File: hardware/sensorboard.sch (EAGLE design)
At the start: 37 parts, among them U1 LM1117MP-3.3, U2 LM324D

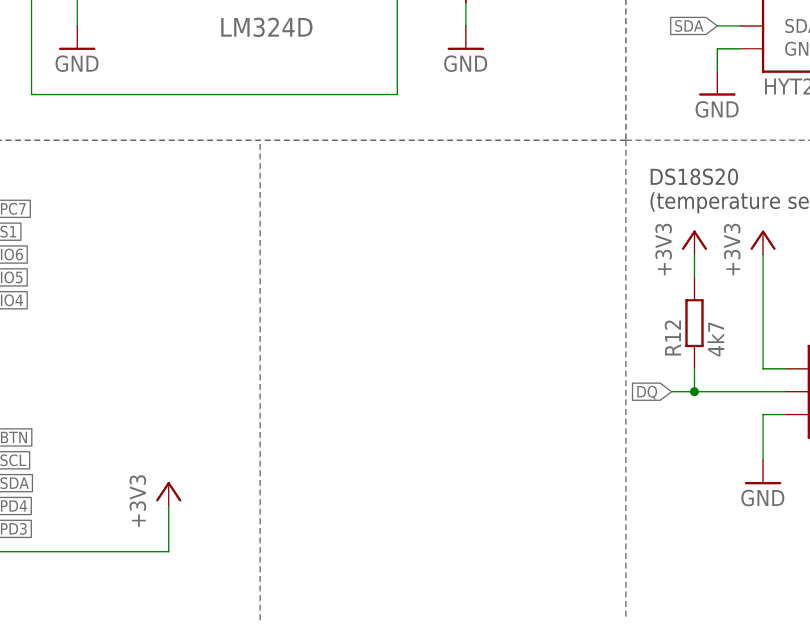
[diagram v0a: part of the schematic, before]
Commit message: added I2C pull up resistors
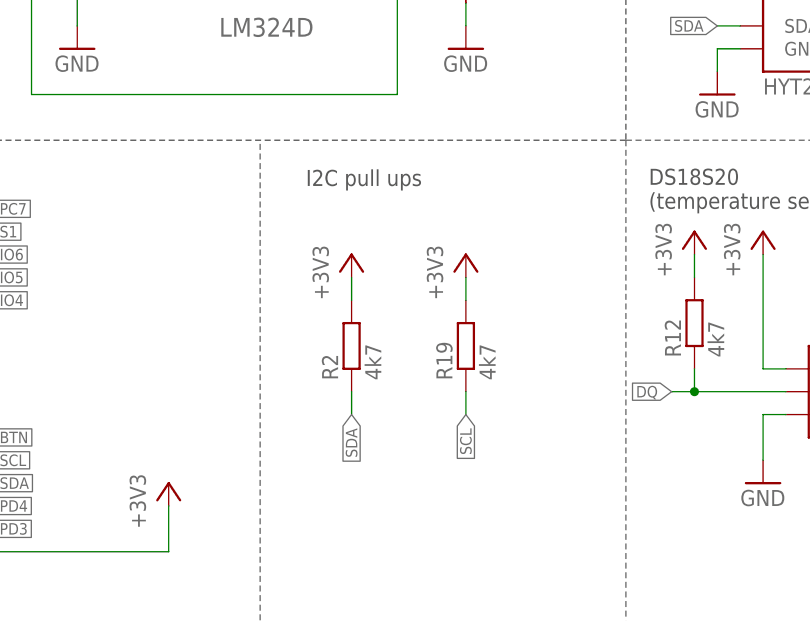
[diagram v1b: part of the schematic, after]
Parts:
- added R19, R2: 4k7, rcl:R-EU_R0805
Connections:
- net +3V3: now also R19.2, R2.2
- net SCL: now also R19.1
- net SDA: now also R2.1
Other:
- note added: "I2C pull ups"
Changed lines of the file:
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@@
 <part name="U$5" library="dallas" deviceset="DS18S20" device=""/>
 <part name="U$3" library="humidity" deviceset="BMP085" device=""/>
+<part name="+3V12" library="supply1" deviceset="+3V3" device=""/>
+<part name="+3V13" library="supply1" deviceset="+3V3" device=""/>
+<part name="R2" library="rcl" deviceset="R-EU_" device="R0805" value="4k7"/>
+<part name="R19" library="rcl" deviceset="R-EU_" device="R0805" value="4k7"/>
 </parts>
 <sheets>
@@
 <wire x1="220.98" y1="78.74" x2="162.56" y2="78.74" width="0.1524" layer="97" style="longdash"/>
 <text x="167.64" y="76.2" size="1.27" layer="97">connectors#</text>
+<text x="93.98" y="53.34" size="1.778" layer="97">I2C pull ups</text>
 </plain>
 <instances>
@@
 <instance part="U$5" gate="G$1" x="154.94" y="30.48"/>
 <instance part="U$3" gate="G$1" x="154.94" y="116.84"/>
+<instance part="+3V12" gate="G$1" x="99.06" y="45.72"/>
+<instance part="+3V13" gate="G$1" x="111.76" y="45.72"/>
+<instance part="R2" gate="G$1" x="99.06" y="35.56" rot="R90"/>
+<instance part="R19" gate="G$1" x="111.76" y="35.56" rot="R90"/>
 </instances>
 <busses>
@@
 <wire x1="134.62" y1="121.92" x2="134.62" y2="124.46" width="0.1524" layer="91"/>
 </segment>
+<segment>
+<pinref part="+3V12" gate="G$1" pin="+3V3"/>
+<pinref part="R2" gate="G$1" pin="2"/>
+<wire x1="99.06" y1="43.18" x2="99.06" y2="40.64" width="0.1524" layer="91"/>
+</segment>
+<segment>
+<pinref part="+3V13" gate="G$1" pin="+3V3"/>
+<pinref part="R19" gate="G$1" pin="2"/>
+<wire x1="111.76" y1="43.18" x2="111.76" y2="40.64" width="0.1524" layer="91"/>
+</segment>
 </net>
 <net name="+5V" class="0">
@@
 <label x="144.78" y="111.76" size="1.27" layer="95" rot="R180" xref="yes"/>
 </segment>
+<segment>
+<pinref part="R2" gate="G$1" pin="1"/>
+<wire x1="99.06" y1="30.48" x2="99.06" y2="27.94" width="0.1524" layer="91"/>
+<label x="99.06" y="27.94" size="1.27" layer="95" rot="R270" xref="yes"/>
+</segment>
 </net>
 <net name="SCL" class="0">
@@
 <label x="144.78" y="114.3" size="1.27" layer="95" rot="R180" xref="yes"/>
 </segment>
-</net>
+<segment>
+<pinref part="R19" gate="G$1" pin="1"/>
+<wire x1="111.76" y1="30.48" x2="111.76" y2="27.94" width="0.1524" layer="91"/>
+<label x="111.76" y="27.94" size="1.27" layer="95" rot="R270" xref="yes"/>
+</segment>
+</net>

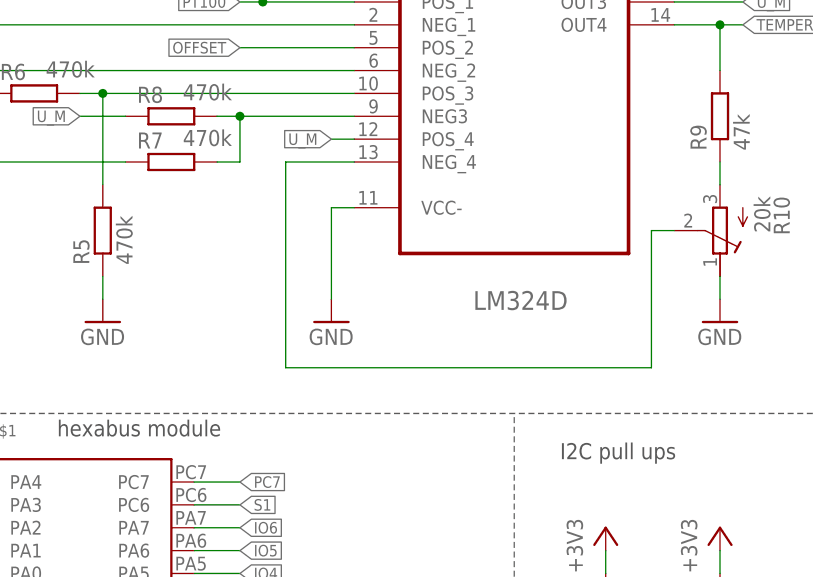
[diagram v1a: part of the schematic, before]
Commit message: added a pinheader for calibrating the measure amplifier. fixes #2
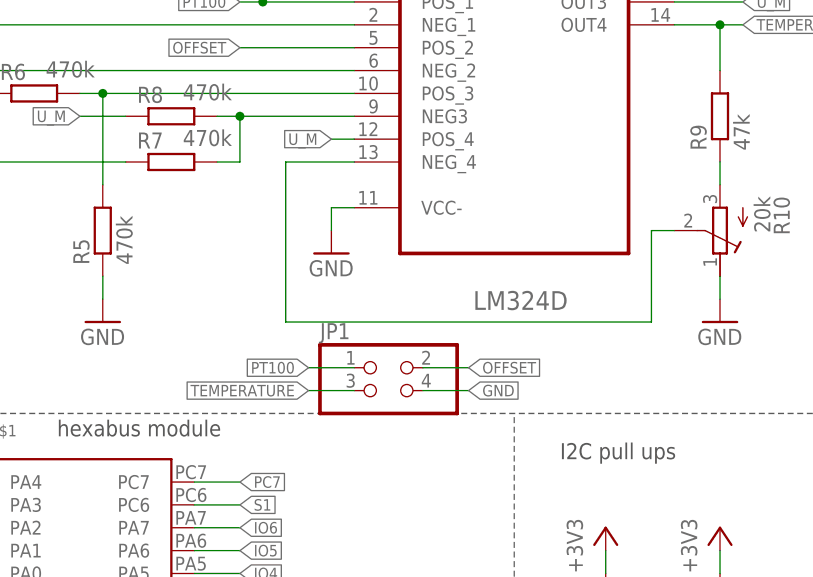
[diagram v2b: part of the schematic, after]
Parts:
- added JP1: (no value), pinhead:PINHD-2X2
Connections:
- net GND: now also JP1.4
- net OFFSET: now also JP1.2
- net PT100: now also JP1.1
- net TEMPERATURE: now also JP1.3
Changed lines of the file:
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@@
 <part name="R2" library="rcl" deviceset="R-EU_" device="R0805" value="4k7"/>
 <part name="R19" library="rcl" deviceset="R-EU_" device="R0805" value="4k7"/>
+<part name="JP1" library="pinhead" deviceset="PINHD-2X2" device=""/>
 </parts>
 <sheets>
@@
 <instance part="U2" gate="A" x="88.9" y="99.06"/>
 <instance part="+3V4" gate="G$1" x="68.58" y="121.92"/>
-<instance part="GND5" gate="1" x="68.58" y="68.58"/>
+<instance part="GND5" gate="1" x="68.58" y="76.2"/>
 <instance part="+3V5" gate="G$1" x="60.96" y="121.92"/>
 <instance part="GND6" gate="1" x="43.18" y="68.58"/>
@@
 <instance part="R2" gate="G$1" x="99.06" y="35.56" rot="R90"/>
 <instance part="R19" gate="G$1" x="111.76" y="35.56" rot="R90"/>
+<instance part="JP1" gate="A" x="76.2" y="60.96"/>
 </instances>
 <busses>
@@
 <pinref part="GND5" gate="1" pin="GND"/>
 <wire x1="71.12" y1="81.28" x2="68.58" y2="81.28" width="0.1524" layer="91"/>
-<wire x1="68.58" y1="81.28" x2="68.58" y2="71.12" width="0.1524" layer="91"/>
+<wire x1="68.58" y1="81.28" x2="68.58" y2="78.74" width="0.1524" layer="91"/>
 </segment>
 <segment>
@@
 <wire x1="139.7" y1="109.22" x2="139.7" y2="104.14" width="0.1524" layer="91"/>
 </segment>
+<segment>
+<pinref part="JP1" gate="A" pin="4"/>
+<wire x1="78.74" y1="60.96" x2="83.82" y2="60.96" width="0.1524" layer="91"/>
+<label x="83.82" y="60.96" size="1.27" layer="95" xref="yes"/>
+</segment>
 </net>
 <net name="+3V3" class="0">
@@
 <label x="182.88" y="55.88" size="1.27" layer="95" rot="R180" xref="yes"/>
 </segment>
+<segment>
+<pinref part="JP1" gate="A" pin="1"/>
+<wire x1="71.12" y1="63.5" x2="66.04" y2="63.5" width="0.1524" layer="91"/>
+<label x="66.04" y="63.5" size="1.27" layer="95" rot="R180" xref="yes"/>
+</segment>
 </net>
 <net name="OFFSET" class="0">
@@
 <wire x1="10.16" y1="101.6" x2="7.62" y2="101.6" width="0.1524" layer="91"/>
 <label x="7.62" y="101.6" size="1.27" layer="95" rot="R90" xref="yes"/>
+</segment>
+<segment>
+<pinref part="JP1" gate="A" pin="2"/>
+<wire x1="78.74" y1="63.5" x2="83.82" y2="63.5" width="0.1524" layer="91"/>
+<label x="83.82" y="63.5" size="1.27" layer="95" xref="yes"/>
 </segment>
 </net>
@@
 <label x="22.86" y="50.8" size="1.27" layer="95" rot="R180" xref="yes"/>
 </segment>
+<segment>
+<pinref part="JP1" gate="A" pin="3"/>
+<wire x1="71.12" y1="60.96" x2="66.04" y2="60.96" width="0.1524" layer="91"/>
+<label x="66.04" y="60.96" size="1.27" layer="95" rot="R180" xref="yes"/>
+</segment>
 </net>
 <net name="N$6" class="0">
@@
 <pinref part="R10" gate="G$1" pin="S"/>
 <wire x1="106.68" y1="78.74" x2="104.14" y2="78.74" width="0.1524" layer="91"/>
-<wire x1="104.14" y1="78.74" x2="104.14" y2="63.5" width="0.1524" layer="91"/>
-<wire x1="104.14" y1="63.5" x2="63.5" y2="63.5" width="0.1524" layer="91"/>
+<wire x1="104.14" y1="78.74" x2="104.14" y2="68.58" width="0.1524" layer="91"/>
+<wire x1="104.14" y1="68.58" x2="63.5" y2="68.58" width="0.1524" layer="91"/>
 <pinref part="U2" gate="A" pin="NEG_4"/>
-<wire x1="63.5" y1="63.5" x2="63.5" y2="86.36" width="0.1524" layer="91"/>
+<wire x1="63.5" y1="68.58" x2="63.5" y2="86.36" width="0.1524" layer="91"/>
 <wire x1="63.5" y1="86.36" x2="71.12" y2="86.36" width="0.1524" layer="91"/>
 </segment>

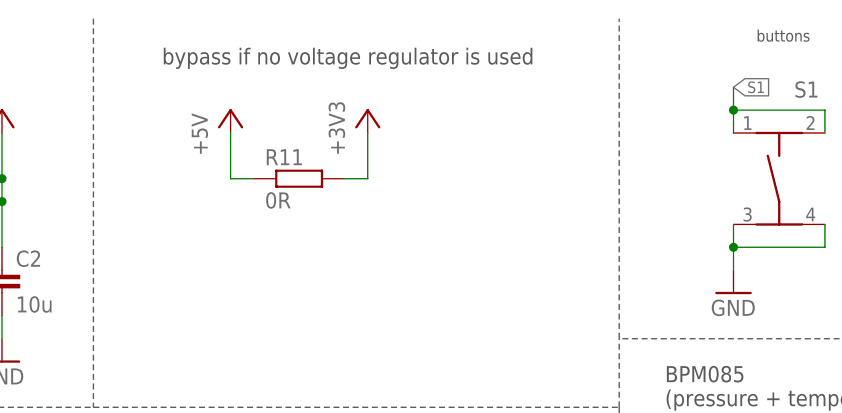
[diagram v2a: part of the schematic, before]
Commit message: removed bypass resistor. see #5
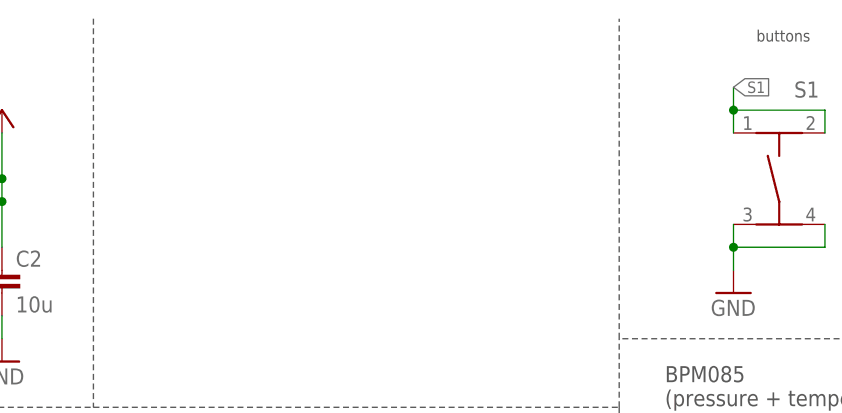
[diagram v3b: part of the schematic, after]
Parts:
- removed R11: 0R, rcl:R-EU_R0805
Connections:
- net +3V3: no longer R11.2
- net +5V: no longer R11.1
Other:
- note removed: "bypass if no voltage regulator is used"
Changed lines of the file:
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@@
 <part name="GND4" library="supply1" deviceset="GND" device=""/>
 <part name="+3V2" library="supply1" deviceset="+3V3" device=""/>
-<part name="+3V3" library="supply1" deviceset="+3V3" device=""/>
-<part name="P+2" library="supply1" deviceset="+5V" device=""/>
 <part name="R1" library="rcl" deviceset="R-EU_" device="R0805" value="1k"/>
 <part name="R3" library="rcl" deviceset="R-EU_" device="R0805" value="100k"/>
 <part name="R5" library="rcl" deviceset="R-EU_" device="R0805" value="470k"/>
 <part name="R6" library="rcl" deviceset="R-EU_" device="R0805" value="470k"/>
-<part name="R11" library="rcl" deviceset="R-EU_" device="R0805" value="0R"/>
 <part name="U2" library="hexasense" deviceset="LM324D" device=""/>
 <part name="+3V4" library="supply1" deviceset="+3V3" device=""/>
@@
 <text x="7.62" y="170.18" size="1.778" layer="97">voltage regulator</text>
 <text x="33.02" y="129.54" size="1.778" layer="97">measure amplifier</text>
-<text x="78.74" y="170.18" size="1.778" layer="97">bypass if no voltage regulator is used</text>
 <wire x1="5.08" y1="132.08" x2="71.12" y2="132.08" width="0.1524" layer="97" style="longdash"/>
 <wire x1="71.12" y1="175.26" x2="71.12" y2="132.08" width="0.1524" layer="97" style="longdash"/>
@@
 <instance part="GND4" gate="1" x="60.96" y="137.16"/>
 <instance part="+3V2" gate="G$1" x="60.96" y="165.1"/>
-<instance part="+3V3" gate="G$1" x="101.6" y="165.1"/>
-<instance part="P+2" gate="1" x="86.36" y="165.1"/>
 <instance part="R1" gate="G$1" x="60.96" y="111.76" rot="R90"/>
 <instance part="R3" gate="G$1" x="15.24" y="114.3" rot="R90"/>
@@
 <attribute name="VALUE" x="36.83" y="95.758" size="1.778" layer="96"/>
 </instance>
-<instance part="R11" gate="G$1" x="93.98" y="157.48"/>
 <instance part="U2" gate="A" x="88.9" y="99.06"/>
 <instance part="+3V4" gate="G$1" x="68.58" y="121.92"/>
@@
 </segment>
 <segment>
-<pinref part="R11" gate="G$1" pin="2"/>
-<pinref part="+3V3" gate="G$1" pin="+3V3"/>
-<wire x1="99.06" y1="157.48" x2="101.6" y2="157.48" width="0.1524" layer="91"/>
-<wire x1="101.6" y1="157.48" x2="101.6" y2="162.56" width="0.1524" layer="91"/>
-</segment>
-<segment>
 <pinref part="U2" gate="A" pin="VCC+"/>
 <pinref part="+3V4" gate="G$1" pin="+3V3"/>
@@
 </segment>
 <segment>
-<pinref part="R11" gate="G$1" pin="1"/>
-<pinref part="P+2" gate="1" pin="+5V"/>
-<wire x1="88.9" y1="157.48" x2="86.36" y2="157.48" width="0.1524" layer="91"/>
-<wire x1="86.36" y1="157.48" x2="86.36" y2="162.56" width="0.1524" layer="91"/>
-</segment>
-<segment>
